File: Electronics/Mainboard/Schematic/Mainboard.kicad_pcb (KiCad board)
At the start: 2 copper layers, 45 x 140 mm, 207 parts, among them J1 CONN_01X02, J10 CONN_01X04, J2 CONN_01X02, J3 CONN_01X02, J4 CONN_01X02, J5 CONN_01X02, J6 CONN_02X05, J7 CONN_02X20, J8 CONN_01X02, J9 CONN_01X02, Q1 PSMN014-40YS, Q2 PSMN014-40YS, Q3 PSMN014-40YS, Q4 PSMN014-40YS, U1 LM2678-3.3V, U10 LTC2954, U2 LM2678-5V, U4 LM5121, U6 ACS781, U7 LSM6DS33, U8 STM32F031G6U6, U9 LTC2876, Y1 Resonator_Small

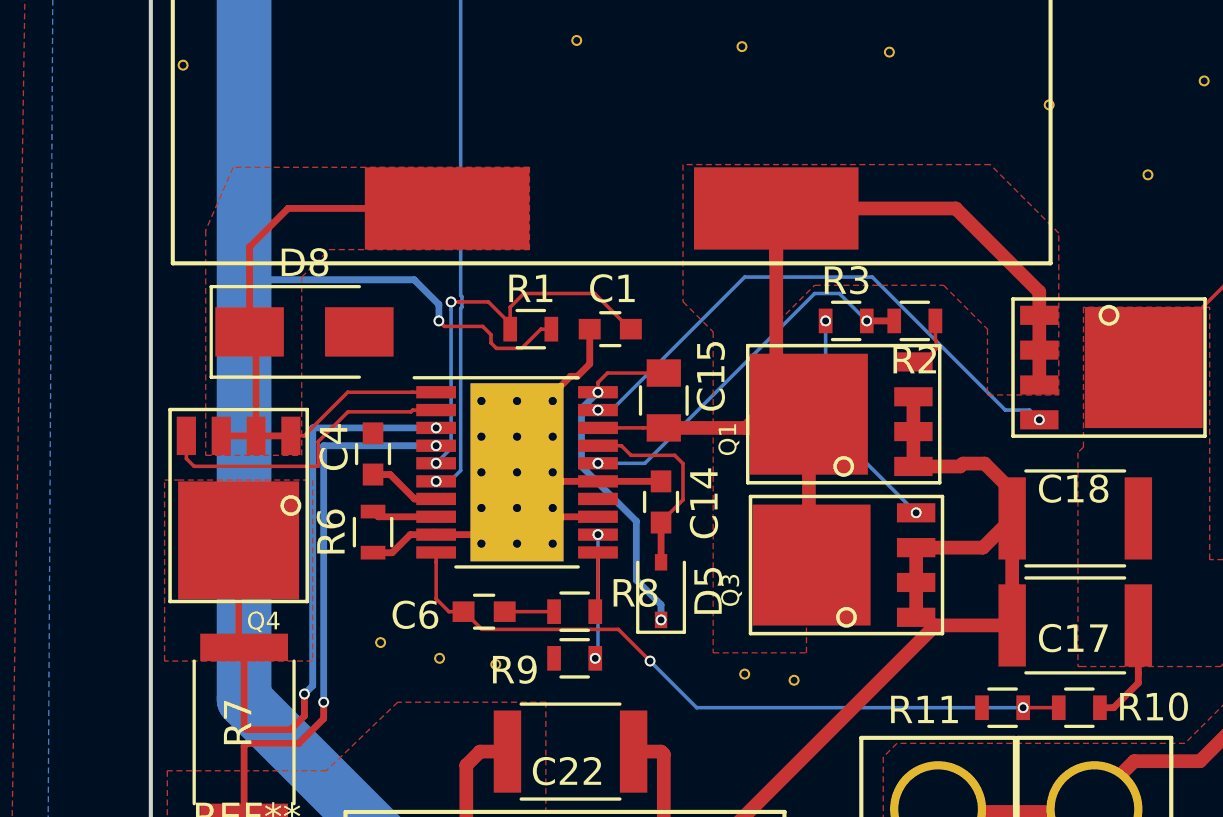
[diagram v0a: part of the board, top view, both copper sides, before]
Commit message: Boost converter calculation
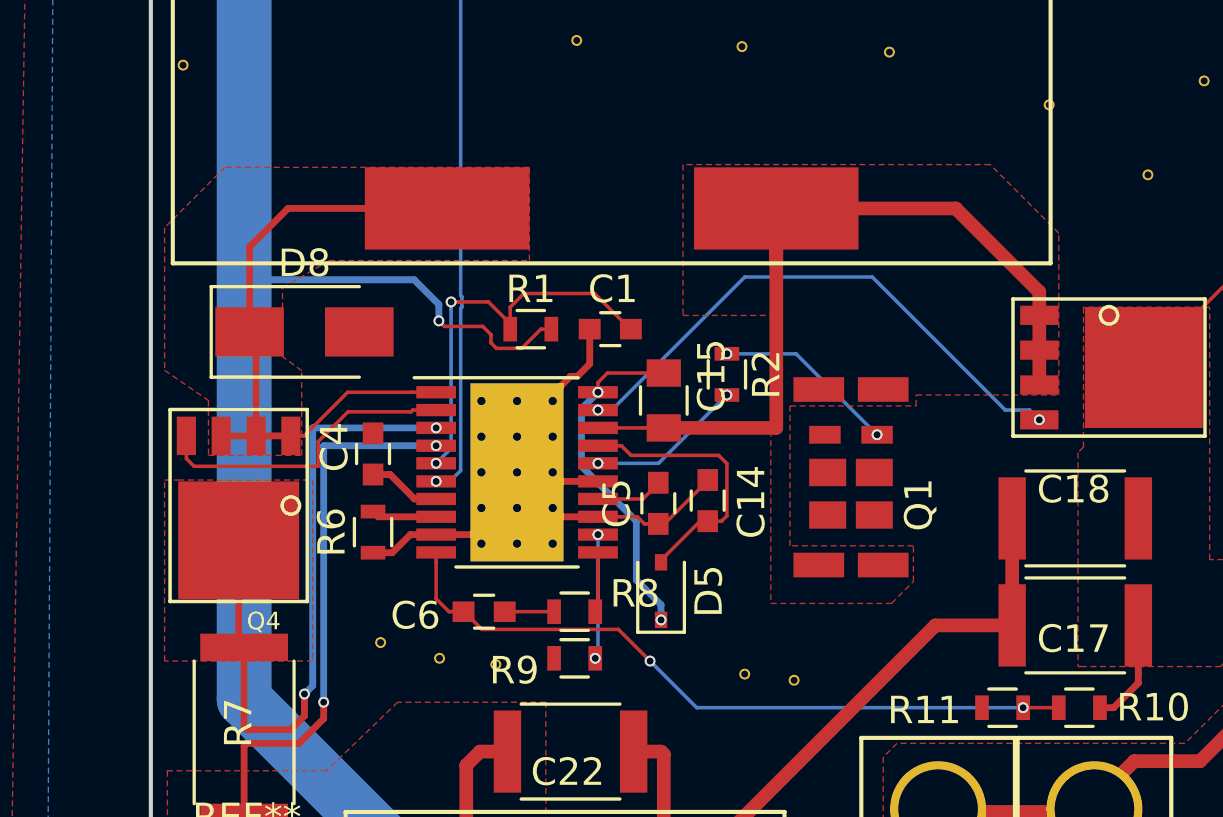
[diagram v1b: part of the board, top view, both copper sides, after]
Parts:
- removed Q3: PSMN014-40YS, Dizzy:PSMN3R3-40YS
- removed R3: 10Ohm, Resistors_SMD:R_0603
- added C5: 3.3uF, Capacitors_SMD:C_0603, F.Cu at (68.5, 150.6)
- C15: value 0.1 -> 0.1uF
- C6: value 0.022uF -> 0.1uF
- L3: value L_Core_Ferrite -> 3.3uH 60A
- Q1: value PSMN014-40YS -> Q_NMOS_DGS; footprint Dizzy:PSMN3R3-40YS -> Dizzy:DirectFET-ME
- R10: value 75k (67, 58) -> 32k
- R6: value 18K -> 30K
- R7: value 1.5mOhm -> 1mOhm
- R8: value 68K -> 2K
- R9: value 30k -> 57K
- moved R2 7.12 mm to (71.0, 145.8), turned to 270 degrees
- moved C14 1.70 mm to (70.3, 150.4)
- moved Q1 1.70 mm to (76.7, 146.4), turned to 270 degrees
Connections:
- Q1 pad 1: Earth -> Net-(C15-Pad1)
- Q1 pad 2: Earth -> Net-(Q1-Pad2)
- R2 pad 1: Net-(Q1-Pad4) -> Net-(Q1-Pad2)
- U4 pad 14: (no net) -> Net-(C5-Pad2)
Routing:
- net Earth: track 89.4 -> 78.8 mm
- net Net-(Q3-Pad4): track 8.36 -> 0.00 mm, vias 2 -> 0
- net Net-(R2-Pad2): track 13.8 -> 5.73 mm
- net Net-(C15-Pad1): track 38.1 -> 30.7 mm
- net Net-(Q1-Pad2): track 0.00 -> 6.70 mm, vias 0 -> 2
- net Net-(C14-Pad1): track 7.30 -> 10.0 mm
- net Net-(C5-Pad2): track 0.00 -> 2.46 mm
- net Net-(Q1-Pad4): track 2.06 -> 0.00 mm

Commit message: started new mainboard
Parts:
- removed REF** (x123): VIA-0.4, Dizzy:VIA-0.4
- removed REF** (x4): MountingHole_3.5mm, Mounting_Holes:MountingHole_3.5mm
- added J11: M1, Dizzy:Hole-m3, F.Cu at (92.4, 164.8)
- added J12: M2, Dizzy:Hole-m3, F.Cu at (53.5, 31.4)
- added J13: M3, Dizzy:Hole-m3, F.Cu at (91.8, 31.7)
- added J14: M4, Dizzy:Hole-m3, F.Cu at (53.4, 164.8)
- added R3: 10Ohm, Resistors_SMD:R_0603, F.Cu at (70.6, 143.2)
- J1, J2, J8, J9: footprint Pin_Headers:Pin_Header_Straight_1x02_Pitch2.54mm -> Dizzy:2x1.5-conn
- J10: footprint Pin_Headers:Pin_Header_Straight_1x04_Pitch2.54mm -> Dizzy:4x1.5-conn
- J3: footprint Dizzy:XT60 -> Dizzy:2x2.1-conn
- J4, J5: footprint Dizzy:xt30 -> Dizzy:2x2.1-conn
- J7: value CONN_02X20 -> CONN_02X10; footprint Pin_Headers:Pin_Header_Straight_2x20_Pitch2.54mm -> Pin_Headers:Pin_Header_Straight_2x10_Pitch2.54mm_SMD
- L2: value 22uH -> 33uH
- Q1: value Q_NMOS_DGS -> BUK7Y7R8-80EX; footprint Dizzy:DirectFET-ME -> Dizzy:PSMN3R3-40YS
- Q2, Q4: value PSMN014-40YS -> BUK7Y7R8-80EX
- U2: value LM2678-5V -> LM2678-12V
- moved J1 12.6 mm to (74.0, 32.0), turned to 0 degrees
- moved J10 8.34 mm to (67.0, 36.5), turned to 180 degrees
- moved Q2 6.00 mm to (78.9, 145.7)
- moved Q1 5.73 mm to (77.2, 152.1), turned to 90 degrees
- moved J7 4.36 mm to (89.2, 53.6)
- moved J2 3.69 mm to (74.1, 36.0), turned to 0 degrees
- moved J8 3.61 mm to (72.3, 81.3), turned to 0 degrees
- moved J9 2.82 mm to (57.5, 81.1), turned to 0 degrees
- moved J3 2.19 mm to (66.6, 167.4)
- moved C17 2.06 mm to (85.8, 154.8)
- moved C18 2.00 mm to (85.7, 151.1)
- moved J5 1.94 mm to (83.3, 165.8)
- moved R10 1.75 mm to (85.6, 158.0)
- moved R11 1.65 mm to (82.7, 158.0)
- moved J4 1.60 mm to (78.7, 165.8)
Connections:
- C13 pad 1: 5V -> 12V
- C29 pad 1: 5V -> 12V
- J7 pad 1: 3.3V -> MOSI
- J7 pad 10: (no net) -> 3.3V
- J7 pad 11: (no net) -> RECVRDY
- J7 pad 12: (no net) -> 3.3V
- J7 pad 13: (no net) -> PWR_INT
- J7 pad 14: Earth -> 3.3V
- J7 pad 15: (no net) -> 5V
- J7 pad 16: GPIO23 -> 12V
- J7 pad 17: 3.3V -> 5V
- J7 pad 18: GPIO24 -> 12V
- J7 pad 19: MOSI -> 5V
- J7 pad 2: (no net) -> ~PWR_KILL
- J7 pad 20: Earth -> 12V
- J7 pad 3: (no net) -> MISO
- J7 pad 4: (no net) -> Earth
- J7 pad 5: (no net) -> SCK
- J7 pad 7: (no net) -> CS
- J7 pad 8: (no net) -> Earth
- J7 pad 9: Earth -> RESPRDY
- L2 pad 2: 5V -> 12V
- Q1 pad 1: Net-(C15-Pad1) -> Earth
- Q1 pad 2: Net-(Q1-Pad2) -> Earth
- R14 pad 2: Net-(C17-Pad1) -> Net-(D8-Pad1)
- R2 pad 1: Net-(Q1-Pad2) -> Net-(Q1-Pad4)
- U2 pad 7: 5V -> 12V
- U4 pad 19: Net-(Q2-Pad4) -> Net-(R3-Pad2)
- U8 pad 15: GPIO19 -> (no net)
- U8 pad 16: GPIO26 -> (no net)
- U8 pad 25: GPIO24 -> (no net)
- U8 pad 26: GPIO23 -> (no net)
- U8 pad 27: GPIO16 -> (no net)
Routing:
- net (no net): track 0.00 -> 234.7 mm, vias 0 -> 7
- net 3.3V: track 251.0 -> 92.1 mm, vias 10 -> 1
- net PWR_BUTTON: track 105.7 -> 18.1 mm
- net +BATT: track 156.7 -> 73.2 mm, vias 22 -> 7
- net V_ADC: track 63.8 -> 10.7 mm
- net GPIO23: track 50.8 -> 0.00 mm, vias 2 -> 0
- net Net-(D8-Pad1): track 23.3 -> 71.6 mm
- net GPIO24: track 47.2 -> 0.00 mm, vias 2 -> 0
- net GPIO26: track 44.9 -> 0.00 mm
- net GPIO16: track 43.0 -> 0.00 mm, vias 2 -> 0
- net GPIO19: track 40.2 -> 0.00 mm
- net Net-(C17-Pad1): track 36.3 -> 4.22 mm
- net 5V: track 23.9 -> 0.00 mm
- net RS-B: track 24.8 -> 7.63 mm
- net RS-A: track 24.1 -> 8.08 mm
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- added copper zone on F.Cu, net 12V
- added copper zone on In1.Cu, net Earth
- added copper zone on F.Cu, net Net-(C8-Pad2)
- removed copper zone on B.Cu, net Earth
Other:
- copper layers 2 -> 4

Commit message: saving
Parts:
- moved U10 74.1 mm to (57.0, 42.3), turned to 180 degrees
- moved R4 69.1 mm to (60.0, 44.0), turned to 90 degrees
- moved C27 67.3 mm to (62.5, 44.0), turned to 90 degrees
- moved R5 11.3 mm to (67.0, 39.1)
- moved J1 5.33 mm to (79.2, 33.5), turned to 180 degrees
- moved J2 5.31 mm to (79.2, 37.6), turned to 180 degrees
- moved J7 2.54 mm to (88.9, 56.2)
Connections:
- J9 pad 2: 5V -> 12V
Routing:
- net (no net): track 234.7 -> 0.00 mm, vias 7 -> 0
- net PWR_EN: track 97.6 -> 156.8 mm, vias 4 -> 5
- net V_ADC: track 10.7 -> 63.3 mm
- net RECVRDY: track 80.9 -> 34.3 mm, vias 2 -> 0
- net +BATT: track 73.2 -> 119.2 mm, vias 7 -> 8
- net 3.3V: track 92.1 -> 51.4 mm, vias 1 -> 18
- net RESPRDY: track 64.1 -> 36.2 mm, vias 2 -> 0
- net ~PWR_KILL: track 13.1 -> 38.5 mm, vias 1 -> 2
- net MOSI: track 30.6 -> 51.9 mm
- net PWR_INT: track 25.5 -> 45.5 mm, vias 1 -> 2
- net MISO: track 32.4 -> 49.2 mm
- net Net-(C10-Pad2): track 15.6 -> 0.00 mm
- net Net-(C3-Pad2): track 14.9 -> 0.00 mm
- net RS-B: track 7.63 -> 21.9 mm
- net PWR_BUTTON: track 18.1 -> 3.97 mm, vias 2 -> 0
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- added copper zone on In2.Cu, net 3.3V
- added copper zone on B.Cu, net Earth
- added copper zone on F.Cu, net Net-(C10-Pad2)
- added copper zone on F.Cu, net Net-(C3-Pad2)
- added copper zone on F.Cu, net Net-(C7-Pad2)
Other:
- board text removed: "A"
- board text removed: "B"
- board text removed: "LED"
- board text removed: "button"

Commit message: new mainboard
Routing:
- net Earth: vias 56 -> 55
- net (no net): vias 0 -> 1
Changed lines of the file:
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@@
     (links 231)
     (no_connects 0)
-    (area 49.924999 29.924999 95.075001 170.075001)
+    (area 47.327142 29.924999 95.075001 170.763333)
     (thickness 1.6)
     (drawings 23)
@@
   )
   (setup
-    (last_trace_width 2)
+    (last_trace_width 0.13)
     (user_trace_width 0.13)
     (user_trace_width 0.25)
@@
     (visible_elements 7FFFEFFF)
     (pcbplotparams
-      (layerselection 0x010f0_80000001)
+      (layerselection 0x010f0_80000007)
       (usegerberextensions false)
       (excludeedgelayer true)
@@
   (gr_line (start 95 32) (end 95 168) (layer Edge.Cuts) (width 0.15))
   (gr_line (start 52 30) (end 93 30) (layer Edge.Cuts) (width 0.15))
+  (via (at 59.45 144.3) (size 1.4) (drill 1) (layers F.Cu B.Cu) (net 0))
   (via (at 54.9 99.6) (size 1.4) (drill 1) (layers F.Cu B.Cu) (net 1))
   (via (at 57.9 99.6) (size 1.4) (drill 1) (layers F.Cu B.Cu) (net 1))
-  (via (at 59.45 144.3) (size 1.4) (drill 1) (layers F.Cu B.Cu) (net 1))
   (segment (start 52.75 84.35) (end 55.35 84.35) (width 2) (layer F.Cu) (net 1))
   (via (at 55.35 84.35) (size 1.4) (drill 1) (layers F.Cu B.Cu) (net 1))
@@
   (segment (start 60.366596 148.45) (end 60.4 148.45) (width 0.25) (layer B.Cu) (net 4))
   (via (at 60.4 148.45) (size 0.4) (drill 0.25) (layers F.Cu B.Cu) (net 4))
+  (segment (start 61.4 154.5) (end 61.425 154.5) (width 0.13) (layer F.Cu) (net 5))
+  (segment (start 61.425 154.5) (end 62.225 155.3) (width 0.13) (layer F.Cu) (net 5))
+  (segment (start 67.2 155.3) (end 68.2 156.3) (width 0.13) (layer F.Cu) (net 5))
+  (segment (start 62.225 155.3) (end 67.2 155.3) (width 0.13) (layer F.Cu) (net 5))
   (segment (start 68.2 156.3) (end 69.1 157.2) (width 0.13) (layer B.Cu) (net 5))
   (segment (start 82.65 157.2) (end 83.45 158) (width 0.13) (layer B.Cu) (net 5))
@@
   (via (at 83.45 158) (size 0.4) (drill 0.25) (layers F.Cu B.Cu) (net 5))
   (segment (start 84.85 158) (end 83.45 158) (width 0.13) (layer F.Cu) (net 5))
-  (segment (start 61.4 154.5) (end 61.425 154.5) (width 0.13) (layer F.Cu) (net 5))
-  (segment (start 61.425 154.5) (end 62.070001 155.145001) (width 0.13) (layer F.Cu) (net 5))
-  (segment (start 62.070001 155.145001) (end 67.045001 155.145001) (width 0.13) (layer F.Cu) (net 5))
-  (segment (start 67.045001 155.145001) (end 68.2 156.3) (width 0.13) (layer F.Cu) (net 5))
   (via (at 68.2 156.3) (size 0.4) (drill 0.25) (layers F.Cu B.Cu) (net 5))
   (segment (start 61.4 154.5) (end 60.87 154.5) (width 0.13) (layer F.Cu) (net 5))
@@
     )
   )
-  (zone (net 1) (net_name Earth) (layer F.Mask) (hatch edge 0.508)
+  (zone (net 0) (net_name "") (layer F.Mask) (hatch edge 0.508)
     (connect_pads (clearance 0.508))
     (min_thickness 0.254)
@@
     )
   )
-  (zone (net 7) (net_name "Net-(C7-Pad2)") (layer F.Mask) (hatch edge 0.508)
+  (zone (net 0) (net_name "") (layer F.Mask) (hatch edge 0.508)
     (connect_pads (clearance 0.508))
     (min_thickness 0.254)

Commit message: body V2
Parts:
- removed C1: 2.2uF, Capacitors_SMD:C_0603
- removed C14, C4: 1uF, Capacitors_SMD:C_0603
- removed C15: 0.1uF, Capacitors_SMD:C_0805
- removed C17, C18: 3.3uF, Capacitors_SMD:C_1812
- removed C5: 3.3uF, Capacitors_SMD:C_0603
- removed C6: 0.1uF, Capacitors_SMD:C_0603
- removed L3: 3.3uH 60A, Dizzy:PQ3218‐3R3‐70‐T
- removed Q4: BUK7Y7R8-80EX, Dizzy:PSMN3R3-40YS
- removed R10: 32k, Resistors_SMD:R_0603
- removed R11: 1k, Resistors_SMD:R_0603
- removed R2, R3: 10Ohm, Resistors_SMD:R_0603
- removed R6: 30K, Resistors_SMD:R_0603
- removed R7: 1mOhm, Resistors_SMD:R_2512
- removed R8: 2K, Resistors_SMD:R_0603
- removed R9: 57K, Resistors_SMD:R_0603
- removed U4: LM5121, Housings_SSOP:HTSSOP-20-1EP_4.4x6.5mm_Pitch0.65mm_ThermalPad
- added J15: CONN_01X01, Dizzy:0.6x1-conn, F.Cu at (60.5, 69.0)
- added J16: CONN_01X01, Dizzy:0.6x1-conn, F.Cu at (53.0, 61.5)
- added J17: CONN_01X01, Dizzy:0.6x1-conn, F.Cu at (81.8, 52.5)
- added J18: CONN_01X01, Dizzy:0.6x1-conn, F.Cu at (82.5, 55.0)
- added J21: CONN_01X01, Dizzy:0.6x1-conn, F.Cu at (55.8, 55.3)
- added J22: CONN_01X01, Dizzy:0.6x1-conn, F.Cu at (55.7, 57.6)
- added J23: CONN_01X01, Dizzy:0.6x1-conn, F.Cu at (60.5, 47.0)
- added J24: CONN_01X01, Dizzy:0.6x1-conn, F.Cu at (81.8, 47.4)
- added J25: CONN_01X01, Dizzy:0.6x1-conn, F.Cu at (81.8, 44.9)
- added J26: CONN_01X01, Dizzy:0.6x1-conn, F.Cu at (81.9, 42.4)
- added J27: CONN_01X01, Dizzy:0.6x1-conn, F.Cu at (81.8, 50.0)
- added U3: ZXTR2012Z, TO_SOT_Packages_SMD:SOT-89-3, F.Cu at (54.5, 76.2)
- C22: value 4.7uF -> 20uF
- D5: footprint Diodes_SMD:D_SOD-323 -> Diodes_SMD:D_SMA
- Q1: value BUK7Y7R8-80EX -> BSS123W; footprint Dizzy:PSMN3R3-40YS -> TO_SOT_Packages_SMD:SOT-323_SC-70
- Q2: value BUK7Y7R8-80EX -> SQJ459EP; footprint Dizzy:PSMN3R3-40YS -> Dizzy:SQJ459EP
- R1: value 3.3 -> 1K
- U10: value LTC2954 -> LTC2954-1
- U8: value STM32F031G6U6 -> STM32F031K6U6
- moved C19 62.1 mm to (53.5, 69.8)
- moved C21 62.1 mm to (58.0, 69.8)
- moved R13 62.1 mm to (53.5, 67.8)
- moved R18 62.1 mm to (58.0, 67.8)
- moved R14 62.1 mm to (53.5, 65.9)
- moved R17 62.1 mm to (58.0, 65.9)
- moved C25 34.8 mm to (58.0, 40.5), turned to 270 degrees
- moved C29 30.3 mm to (92.5, 111.1)
- moved C9 30.1 mm to (92.2, 117.8)
- moved C13 29.4 mm to (88.2, 111.2)
- moved C3 29.3 mm to (88.0, 117.9)
- moved D3 28.0 mm to (80.3, 119.5), turned to 270 degrees
- moved U2 27.3 mm to (83.1, 109.2)
- moved J9 27.1 mm to (83.8, 87.8)
- moved L2 26.8 mm to (85.9, 99.9)
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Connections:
- D5 pad 1: Net-(C15-Pad2) -> +90V
- D5 pad 2: Net-(C14-Pad1) -> Earth
- D8 pad 1: Net-(D8-Pad1) -> +90V
- Q1 pad 1: Earth -> PWR_EN
- Q1 pad 3: Earth -> Net-(Q1-Pad3)
- Q2 pad 1: Net-(C15-Pad1) -> +BATT
- Q2 pad 2: Net-(C15-Pad1) -> Net-(Q1-Pad3)
- Q2 pad 3: Net-(C15-Pad1) -> Net-(Q2-Pad3)
- R1 pad 1: Net-(C1-Pad1) -> Net-(Q1-Pad3)
- R14 pad 2: Net-(D8-Pad1) -> +BATT
- U10 pad 4: +BATT -> Net-(U10-Pad4)
- U6 pad 5: Net-(C17-Pad1) -> Net-(Q2-Pad3)
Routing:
- net Net-(R17-Pad1): track 34.2 -> 105.9 mm, vias 0 -> 2
- net Net-(D8-Pad1): track 64.8 -> 0.00 mm
- net Earth: track 67.8 -> 128.1 mm, vias 55 -> 91
- net I_ADC: track 72.6 -> 24.1 mm, vias 4 -> 2
- net Net-(U10-Pad4): track 0.00 -> 40.3 mm, vias 0 -> 2
- net V_ADC: track 63.3 -> 28.1 mm
- net MOSI: track 51.9 -> 23.3 mm, vias 2 -> 0
- net Net-(C6-Pad2): track 27.8 -> 0.00 mm, vias 2 -> 0
- net MISO: track 49.2 -> 22.4 mm, vias 2 -> 0
- net Net-(Q4-Pad5678): track 25.1 -> 0.00 mm, vias 2 -> 0
- net SCK: track 46.5 -> 22.0 mm, vias 2 -> 0
- net CS: track 43.8 -> 21.7 mm, vias 2 -> 0
- net Net-(Q1-Pad3): track 0.00 -> 22.0 mm, vias 0 -> 2
- net Net-(C15-Pad1): track 19.0 -> 0.00 mm
- net RECVRDY: track 34.3 -> 50.0 mm, vias 0 -> 1
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- added copper zone on F.Cu, net 3.3V
- added copper zone on F.Cu, net Net-(Q2-Pad3)
- removed copper zone on B.Cu, net +BATT
- removed copper zone on B.Cu, net Earth
- removed copper zone on F.Cu, net Net-(C15-Pad1)
- removed copper zone on F.Cu, net Net-(C17-Pad1)
- removed copper zone on F.Cu, net Net-(D8-Pad1)
- removed copper zone on F.Cu, net Net-(Q4-Pad5678)
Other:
- board text removed: "+"
- board text removed: "-"
- board text removed: "12-24 V supply"
- board text removed: "3.3V"
- board text removed: "5V"
- board text removed: "90 V output"
- board text removed: "GND"
